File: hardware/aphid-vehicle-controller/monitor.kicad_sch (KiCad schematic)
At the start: 2 parts, among them J3 MONITOR_DEBUG, U4 STM32F091CCTx

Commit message: more work on pcb
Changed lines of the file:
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@@
+		)
+	)
+	(hierarchical_label "ENABLE_RESET"
+		(shape output)
+		(at 207.01 132.08 0)
+		(fields_autoplaced yes)
+		(effects
+			(font
+				(size 1.27 1.27)
+			)
+			(justify left)
 		)
 	)

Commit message: worked on VCM
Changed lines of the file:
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@@
 		)
 	)
-	(hierarchical_label "ACC1_FILTERED"
+	(hierarchical_label "MONITOR_UART_TX"
+		(shape output)
+		(at 59.69 83.82 0)
+		(fields_autoplaced yes)
+		(effects
+			(font
+				(size 1.27 1.27)
+			)
+			(justify left)
+		)
+	)
+	(hierarchical_label "DIR_F"
+		(shape input)
+		(at 205.74 120.65 0)
+		(fields_autoplaced yes)
+		(effects
+			(font
+				(size 1.27 1.27)
+			)
+			(justify left)
+		)
+	)
+	(hierarchical_label "ACC"
 		(shape input)
 		(at 204.47 110.49 0)
@@
 		)
 	)
-	(hierarchical_label "ACC2_FILTERED"
+	(hierarchical_label "HIGH_SIDE_SENSE"
 		(shape input)
-		(at 204.47 119.38 0)
+		(at 214.63 101.6 0)
 		(fields_autoplaced yes)
 		(effects
@@
 		)
 	)
-	(hierarchical_label "ENABLE_RESET"
-		(shape output)
-		(at 207.01 132.08 0)
+	(hierarchical_label "BRAKE"
+		(shape input)
+		(at 204.47 115.57 0)
 		(fields_autoplaced yes)
 		(effects
@@
 		)
 	)
+	(hierarchical_label "MONITOR_UART_RX"
+		(shape input)
+		(at 59.69 88.9 0)
+		(fields_autoplaced yes)
+		(effects
+			(font
+				(size 1.27 1.27)
+			)
+			(justify left)
+		)
+	)
+	(hierarchical_label "DIR_R"
+		(shape input)
+		(at 204.47 124.46 0)
+		(fields_autoplaced yes)
+		(effects
+			(font
+				(size 1.27 1.27)
+			)
+			(justify left)
+		)
+	)
 	(hierarchical_label "CAN1_MONITOR_RX"
 		(shape input)
@@
 		(fields_autoplaced yes)
 		(effects
+			(font
+				(size 1.27 1.27)
+			)
+			(justify left)
+		)
+	)
+	(hierarchical_label "CRANK_SENSE"
+		(shape input)
+		(at 205.74 128.27 0)
+		(fields_autoplaced yes)
+		(effects

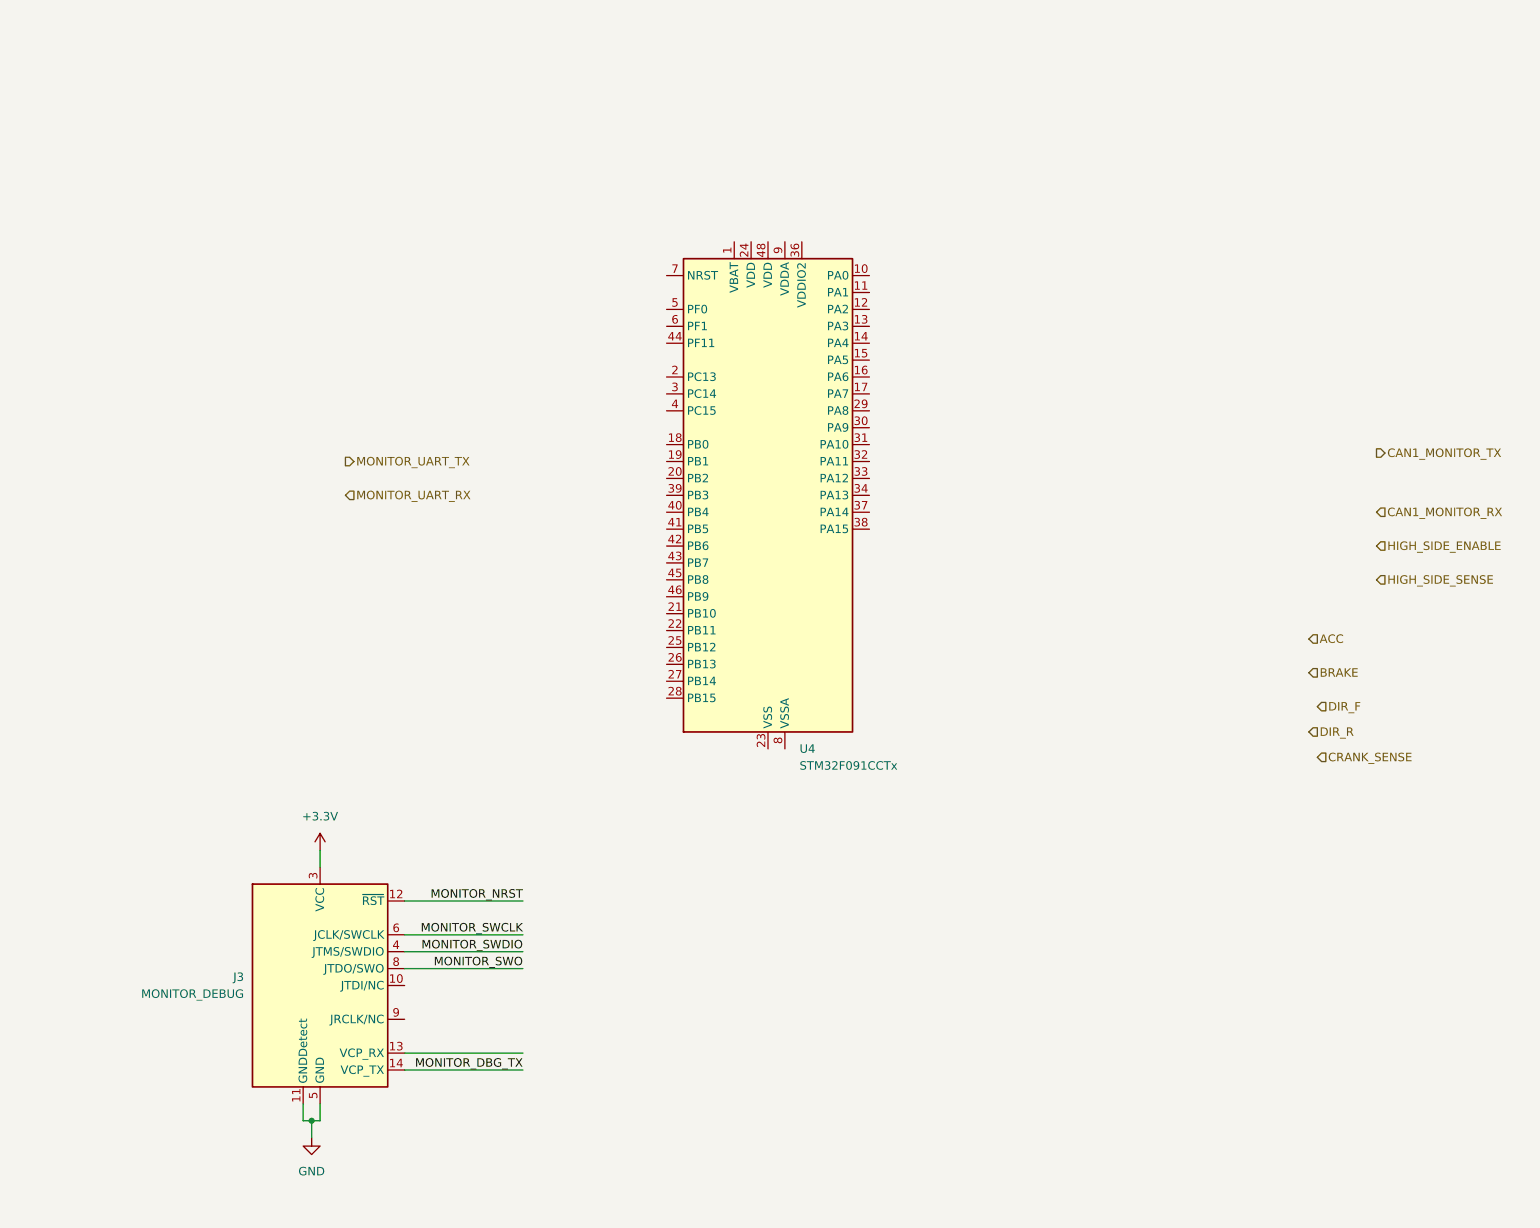
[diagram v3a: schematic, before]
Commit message: feat: changed to STM32G4xx series MCU
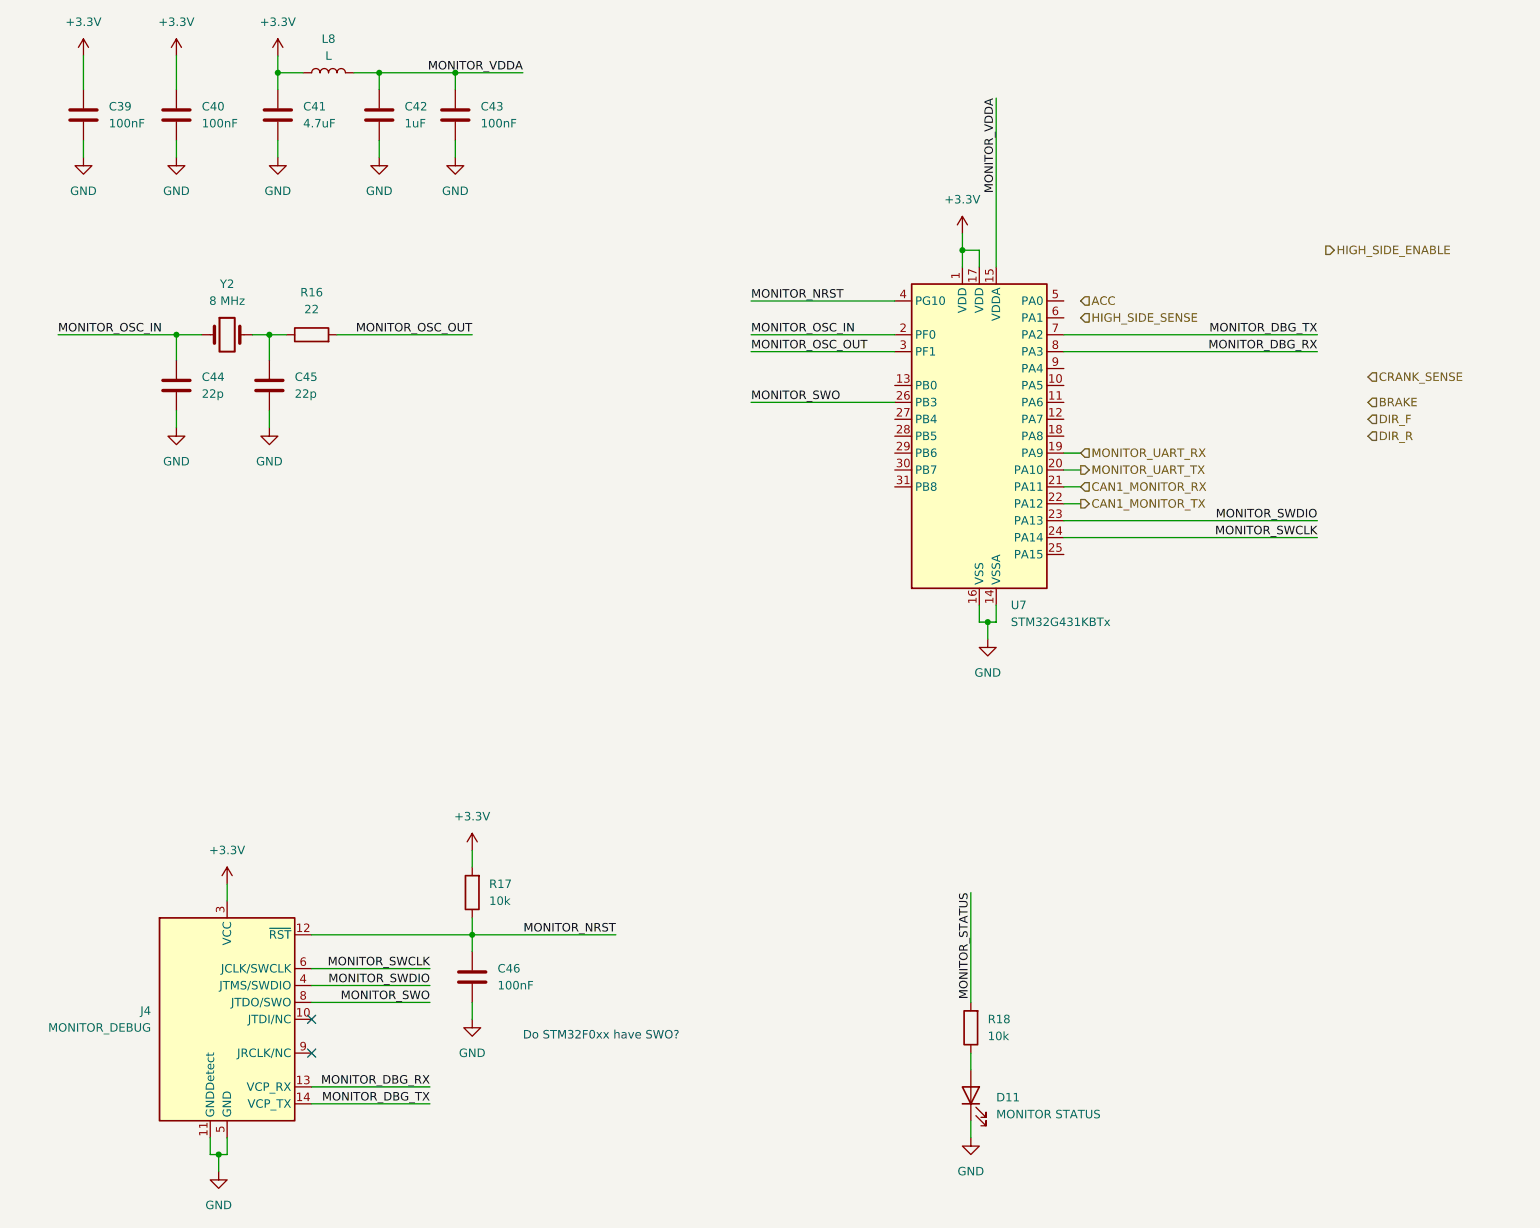
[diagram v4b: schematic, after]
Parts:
- removed U4: STM32F091CCTx, Package_QFP:LQFP-48_7x7mm_P0.5mm, symbol MCU_ST_STM32F0:STM32F091CCTx
- added C39, C40, C43, C46: 100nF, Capacitor_SMD:C_0603_1608Metric, symbol Device:C
- added C41: 4.7uF, Capacitor_SMD:C_0805_2012Metric, symbol Device:C
- added C42: 1uF, Capacitor_SMD:C_0603_1608Metric, symbol Device:C
- added C44, C45: 22p, Capacitor_SMD:C_0603_1608Metric, symbol Device:C
- added D11: MONITOR STATUS, LED_SMD:LED_0603_1608Metric, symbol Device:LED
- added L8: L, Inductor_SMD:L_0805_2012Metric, symbol Device:L
- added R16: 22, Resistor_SMD:R_0603_1608Metric, symbol Device:R
- added R17, R18: 10k, Resistor_SMD:R_0603_1608Metric, symbol Device:R
- added U7: STM32G431KBTx, Package_QFP:LQFP-32_7x7mm_P0.8mm, symbol MCU_ST_STM32G4:STM32G431KBTx
- added Y2: 8 MHz, aphid:ABM3-x.xxxMHZ-D2Y-T, symbol Device:Crystal
- J4: renamed from J3; footprint (none) -> Connector_PinHeader_1.27mm:PinHeader_2x07_P1.27mm_Vertical_SMD
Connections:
- net +3.3V: now also C39.1, C40.1, C41.1, L8.1, R17.2, U7.1 (VDD), U7.17 (VDD)
- net CAN1_MONITOR_RX: now also U7.21 (PA11)
- net CAN1_MONITOR_TX: now also U7.22 (PA12)
- net GND: now also C39.2, C40.2, C41.2, C42.2, C43.2, C44.2, C45.2, C46.2, D11.1 (K), U7.14 (VSSA), U7.16 (VSS), U7.32 (VSS)
- net MONITOR_DBG_TX: now also U7.7 (PA2)
- net MONITOR_NRST: now also C46.1, R17.1, U7.4 (PG10)
- net MONITOR_SWCLK: now also U7.24 (PA14)
- net MONITOR_SWDIO: now also U7.23 (PA13)
- net MONITOR_SWO: now also U7.26 (PB3)
- net MONITOR_UART_RX: now also U7.19 (PA9)
- net MONITOR_UART_TX: now also U7.20 (PA10)
- net MONITOR_DBG_RX: now reaches J4.13 (VCP_RX)
- net MONITOR_DBG_RX: now also U7.8 (PA3)
- new net: C45.1, R16.1, Y2.2
- new net: D11.2 (A), R18.1
- new net MONITOR_OSC_IN: C44.1, U7.2 (PF0), Y2.1
- new net MONITOR_OSC_OUT: R16.2, U7.3 (PF1)
- new net MONITOR_STATUS: R18.2
- new net MONITOR_VDDA: C42.1, C43.1, L8.2, U7.15 (VDDA)
- no-connect marks 0 -> 2
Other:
- note added: "Do STM32F0xx have SWO?"
- moved on the sheet: J4

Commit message: feat: changed to a more modern DCDC
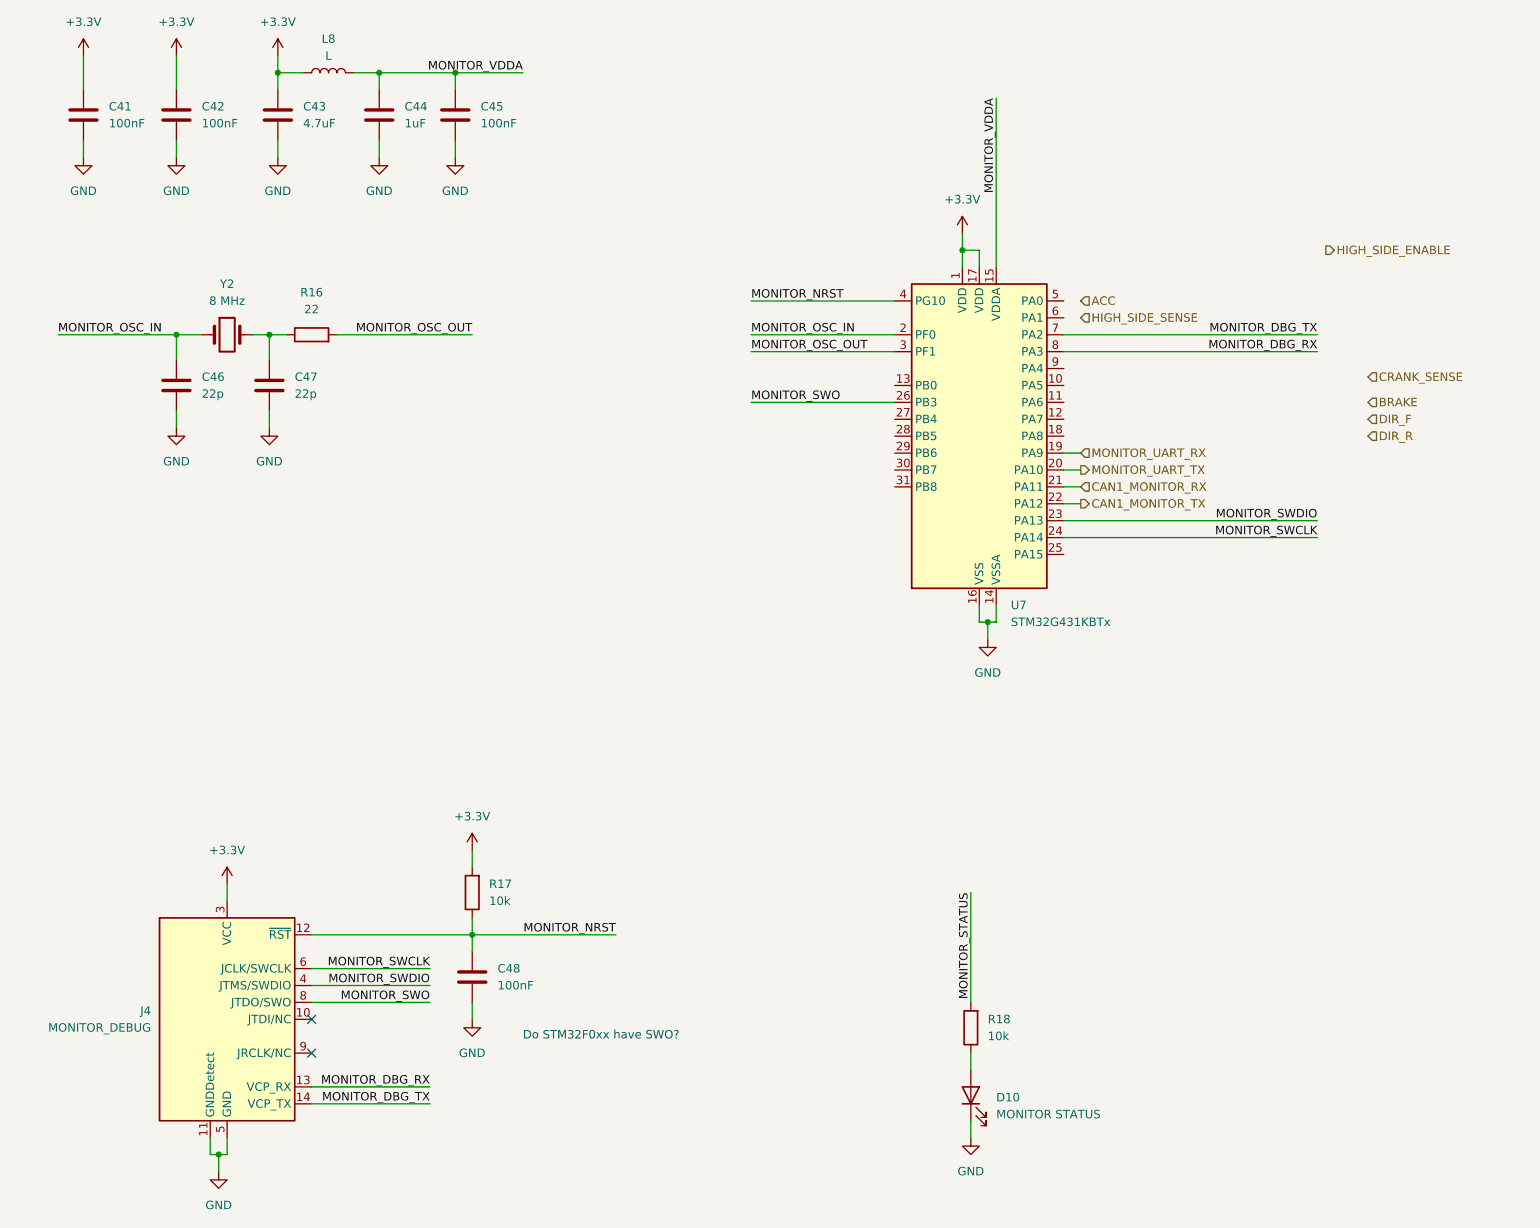
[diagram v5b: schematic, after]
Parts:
- renumbered C39 to C41, C40 to C42, C41 to C43, C42 to C44, C43 to C45, C44 to C46, C45 to C47, C46 to C48, D11 to D10
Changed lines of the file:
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@@
 		(dnp no)
 		(fields_autoplaced yes)
-		(property "Reference" "C41"
+		(property "Reference" "C43"
 			(at 53.34 30.4799 0)
 			(effects
@@
 			(project "aphid-vehicle-controller"
 				(path "/1bdad060-e59b-443f-afdb-9aa678a43546/de3f6686-136b-4e72-913e-b14f46f4b1e0"
-					(reference "C41")
+					(reference "C43")
 					(unit 1)
 				)
@@
 		(dnp no)
 		(fields_autoplaced yes)
-		(property "Reference" "C39"
+		(property "Reference" "C41"
 			(at 24.13 30.4799 0)
 			(effects
@@
 			(project "aphid-vehicle-controller"
 				(path "/1bdad060-e59b-443f-afdb-9aa678a43546/de3f6686-136b-4e72-913e-b14f46f4b1e0"
-					(reference "C39")
+					(reference "C41")
 					(unit 1)
 				)
@@
 		(dnp no)
 		(fields_autoplaced yes)
-		(property "Reference" "C46"
+		(property "Reference" "C48"
 			(at 82.55 160.0199 0)
 			(effects
@@
 			(project "aphid-vehicle-controller"
 				(path "/1bdad060-e59b-443f-afdb-9aa678a43546/de3f6686-136b-4e72-913e-b14f46f4b1e0"
-					(reference "C46")
+					(reference "C48")
 					(unit 1)
 				)
@@
 		(dnp no)
 		(fields_autoplaced yes)
-		(property "Reference" "C43"
+		(property "Reference" "C45"
 			(at 80.01 30.4799 0)
 			(effects
@@
 			(project "aphid-vehicle-controller"
 				(path "/1bdad060-e59b-443f-afdb-9aa678a43546/de3f6686-136b-4e72-913e-b14f46f4b1e0"
-					(reference "C43")
+					(reference "C45")
 					(unit 1)
 				)
@@
 		(dnp no)
 		(fields_autoplaced yes)
-		(property "Reference" "C42"
+		(property "Reference" "C44"
 			(at 68.58 30.4799 0)
 			(effects
@@
 			(project "aphid-vehicle-controller"
 				(path "/1bdad060-e59b-443f-afdb-9aa678a43546/de3f6686-136b-4e72-913e-b14f46f4b1e0"
-					(reference "C42")
+					(reference "C44")
 					(unit 1)
 				)
@@
 		(dnp no)
 		(fields_autoplaced yes)
-		(property "Reference" "C45"
+		(property "Reference" "C47"
 			(at 52.07 71.1199 0)
 			(effects
@@
 			(project "aphid-vehicle-controller"
 				(path "/1bdad060-e59b-443f-afdb-9aa678a43546/de3f6686-136b-4e72-913e-b14f46f4b1e0"
-					(reference "C45")
+					(reference "C47")
 					(unit 1)
 				)
@@
 		(dnp no)
 		(fields_autoplaced yes)
-		(property "Reference" "D11"
+		(property "Reference" "D10"
 			(at 157.48 179.3874 90)
 			(effects
@@
 			(project ""
 				(path "/1bdad060-e59b-443f-afdb-9aa678a43546/de3f6686-136b-4e72-913e-b14f46f4b1e0"
-					(reference "D11")
+					(reference "D10")
 					(unit 1)
 				)
@@
 		(dnp no)
 		(fields_autoplaced yes)
-		(property "Reference" "C44"
+		(property "Reference" "C46"
 			(at 38.1 71.1199 0)
 			(effects
@@
 			(project "aphid-vehicle-controller"
 				(path "/1bdad060-e59b-443f-afdb-9aa678a43546/de3f6686-136b-4e72-913e-b14f46f4b1e0"
-					(reference "C44")
+					(reference "C46")
 					(unit 1)
 				)
@@
 		(dnp no)
 		(fields_autoplaced yes)
-		(property "Reference" "C40"
+		(property "Reference" "C42"
 			(at 38.1 30.4799 0)
 			(effects
@@
 			(project "aphid-vehicle-controller"
 				(path "/1bdad060-e59b-443f-afdb-9aa678a43546/de3f6686-136b-4e72-913e-b14f46f4b1e0"
-					(reference "C40")
-					(unit 1)
-				)
+					(reference "C42")
+					(unit 1)
+				)

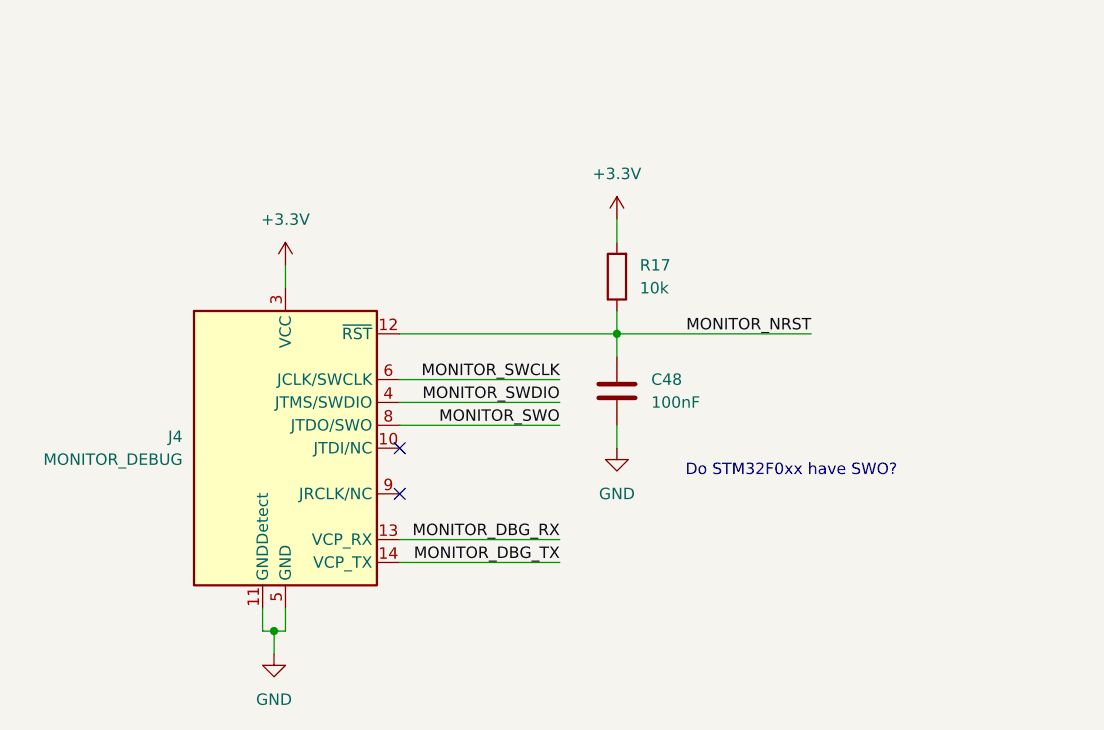
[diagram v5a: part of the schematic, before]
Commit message: Changed debug connector to tagconnect
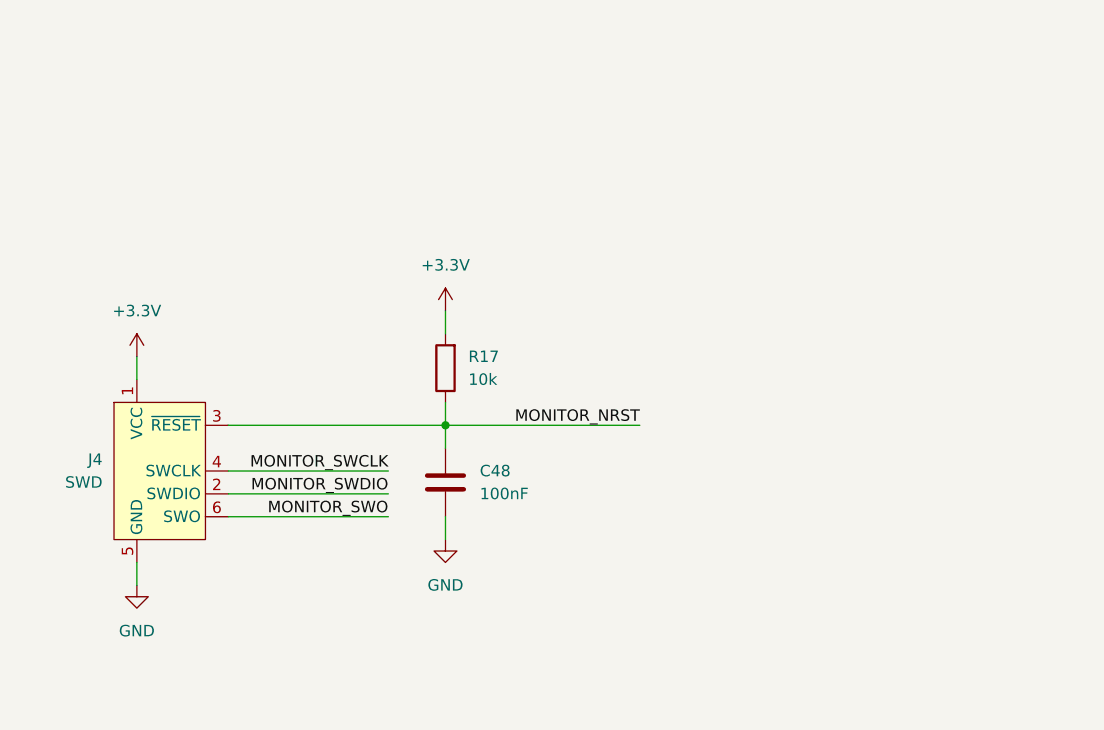
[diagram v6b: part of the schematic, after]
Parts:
- removed J4: MONITOR_DEBUG, Connector_PinHeader_1.27mm:PinHeader_2x07_P1.27mm_Vertical_SMD, symbol Connector:Conn_ST_STDC14
- added J4: SWD, Connector:Tag-Connect_TC2030-IDC-FP_2x03_P1.27mm_Vertical, symbol Connector:Conn_ARM_SWD_TagConnect_TC2030
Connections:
- net +3.3V: now also J4.1 (VCC)
- net GND: now also J4.5 (GND)
- net MONITOR_NRST: now also J4.3 (~{RESET})
- net MONITOR_SWCLK: now also J4.4 (SWCLK)
- net MONITOR_SWDIO: now also J4.2 (SWDIO)
- net MONITOR_SWO: now also J4.6 (SWO)
- no-connect marks 2 -> 0
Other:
- note removed: "Do STM32F0xx have SWO?"
- moved on the sheet: C48, R17
